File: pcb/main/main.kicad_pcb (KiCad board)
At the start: 2 copper layers, 91 x 94.8 mm, 71 parts, among them J1 XT60PW-M, J10 Conn, J11 Conn_ARM_JTAG_SWD_10, J12 UART1 SH, J13 Micro_SD_Card, J14 PH 2.0, J2 Conn_01x06_Female, J3 Conn_01x06_Female, J4 Conn_01x06_Female, J5 Conn_01x06_Female, J6 Conn_01x06_Female, J7 Conn_01x06_Female, J8 Conn, J9 Conn, Q1 BSS138, SW1 RESET, SW2 USER, U1 NJM12877F33-TE1, U2 STM32F405RGTx, U3 MCP2562-E-SN, U4 LXDC55FAAA-203, Y1 XRCGB16M000FXN02R0

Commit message: feat: finish main board v2
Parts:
- removed the C1 at (153.7, 116.5)
- removed the C2 at (151.7, 116.5)
- removed the R9 at (165.6, 95.2)
- removed the U1 at (148.2, 116.7)
- added D1: LED, LED_SMD:LED_0603_1608Metric, F.Cu at (143.2, 136.3)
- added H1: MountingHole, MountingHole:MountingHole_3.2mm_M3_Pad_TopBottom, F.Cu at (94.5, 51.3)
- added H2: MountingHole, MountingHole:MountingHole_3.2mm_M3_Pad_TopBottom, F.Cu at (179.5, 51.3)
- added H3: MountingHole, MountingHole:MountingHole_3.2mm_M3_Pad_TopBottom, F.Cu at (94.5, 140.1)
- added H4: MountingHole, MountingHole:MountingHole_3.2mm_M3_Pad_TopBottom, F.Cu at (179.5, 140.1)
- added H5: MountingHole, MountingHole:MountingHole_2.2mm_M2_ISO14580_Pad, F.Cu at (119.5, 103.4)
- added H6: MountingHole, MountingHole:MountingHole_2.2mm_M2_ISO14580_Pad, F.Cu at (138.1, 103.4)
- added H7: MountingHole, MountingHole:MountingHole_2.2mm_M2_ISO14580_Pad, F.Cu at (138.1, 130.1)
- added H8: MountingHole, MountingHole:MountingHole_2.2mm_M2_ISO14580_Pad, F.Cu at (119.5, 130.1)
- added R16: 120, Resistor_SMD:R_0603_1608Metric_Pad0.98x0.95mm_HandSolder, F.Cu at (164.8, 95.2)
- added R17: 120, Resistor_SMD:R_0603_1608Metric_Pad0.98x0.95mm_HandSolder, F.Cu at (94.2, 102.2)
- added R2: 1k, Resistor_SMD:R_0603_1608Metric_Pad0.98x0.95mm_HandSolder, F.Cu at (143.2, 139.6)
- added R25: 12k, Resistor_SMD:R_0603_1608Metric, F.Cu at (146.9, 125.5)
- added R26: 33k, Resistor_SMD:R_0603_1608Metric, F.Cu at (146.9, 122.4)
- added U2: LT1963AES3-3.3, Package_TO_SOT_SMD:SOT-223, F.Cu at (150.4, 111.6)
- C1: renamed from C17; moved to F.Cu
- C2: renamed from C18; footprint Capacitor_SMD:C_0603_1608Metric_Pad1.08x0.95mm_HandSolder -> Capacitor_SMD:C_0805_2012Metric_Pad1.18x1.45mm_HandSolder
- C3: value 0.01u -> 10u; footprint Capacitor_SMD:C_0603_1608Metric_Pad1.08x0.95mm_HandSolder -> Capacitor_SMD:C_0805_2012Metric_Pad1.18x1.45mm_HandSolder
- C4: value 1u -> 10u; footprint Capacitor_SMD:C_0603_1608Metric_Pad1.08x0.95mm_HandSolder -> Capacitor_SMD:C_0805_2012Metric_Pad1.18x1.45mm_HandSolder
- C5: renamed from C19; footprint Capacitor_SMD:C_0603_1608Metric_Pad1.08x0.95mm_HandSolder -> Capacitor_SMD:C_0805_2012Metric_Pad1.18x1.45mm_HandSolder
- D2: renamed from D1; footprint LED_SMD:LED_0402_1005Metric -> LED_SMD:LED_0603_1608Metric
- D3: renamed from D2; footprint LED_SMD:LED_0402_1005Metric -> LED_SMD:LED_0603_1608Metric
- D4: renamed from D3; footprint LED_SMD:LED_0402_1005Metric -> LED_SMD:LED_0603_1608Metric
- D5: renamed from D4; footprint LED_SMD:LED_0402_1005Metric -> LED_SMD:LED_0603_1608Metric
- D6: renamed from D5; footprint LED_SMD:LED_0402_1005Metric -> LED_SMD:LED_0603_1608Metric
- D7: renamed from D6; footprint LED_SMD:LED_0402_1005Metric -> LED_SMD:LED_0603_1608Metric
- D8: renamed from D7; footprint LED_SMD:LED_0402_1005Metric -> LED_SMD:LED_0603_1608Metric
- J1: footprint Connector_AMASS:AMASS_XT30U-F_1x02_P5.0mm_Vertical -> Connector_AMASS:AMASS_XT60PW-F_1x02_P7.20mm_Horizontal; moved to F.Cu
- J13: renamed from J11; footprint Connector_PinHeader_1.27mm:PinHeader_2x05_P1.27mm_Vertical -> mylib:322110010000
- J14: renamed from J12; footprint Connector_PinHeader_2.54mm:PinHeader_1x04_P2.54mm_Horizontal -> Connector_PinHeader_2.54mm:PinHeader_1x04_P2.54mm_Vertical
- R1: renamed from R22; footprint Resistor_SMD:R_0603_1608Metric_Pad0.98x0.95mm_HandSolder -> Resistor_SMD:R_0805_2012Metric
- moved SP1 58.4 mm to (89.8, 112.1), turned to 90 degrees
- moved R18 50.4 mm to (94.2, 103.7)
- moved Q1 50.4 mm to (94.2, 107.2)
- moved D6 19.7 mm to (135.9, 139.6)
- moved R15 19.7 mm to (135.9, 136.4)
- moved C1 18.5 mm to (160.4, 120.0), turned to 180 degrees
- moved C2 17.5 mm to (165.9, 113.4)
- moved C5 17.5 mm to (165.9, 109.9)
- moved R1 17.5 mm to (157.0, 110.6)
- moved U1 17.5 mm to (161.6, 111.5)
- moved D5 13.4 mm to (132.8, 139.7)
- moved R13 13.4 mm to (132.8, 136.4)
- moved J12 13.1 mm to (119.0, 117.1), turned to 90 degrees
- moved D2 12.7 mm to (140.6, 136.3), turned to 90 degrees
- moved J1 12.4 mm to (156.9, 127.2), turned to 180 degrees
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- renumbered C11 to C10, C12 to C11, C13 to C12, C14 to C13, C15 to C14, C5 to C15, C8 to C16, C16 to C17, C9 to C8, C10 to C9, J13 to J11, J14 to J12, R4 to R10, R5 to R11, R6 to R12, R7 to R13, R3 to R14, R8 to R15, R10 to R18, R11 to R19, R12 to R20, R13 to R21, R14 to R22, R15 to R23, R16 to R24, R1 to R3, R2 to R4, R17 to R5, R18 to R6, R19 to R7, R20 to R8, R21 to R9, U4 to U1, U2 to U3, U3 to U4
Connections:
- C3 pad 1: Net-(C3-Pad1) -> +5V
- J12 pad 1: +5V -> +3.3V
- Q1 pad 1: /stm32f405rg/TIM12_SP -> Net-(Q1-G)
- R18 pad 1: /stm32f405rg/TIM12_SP -> Net-(Q1-G)
- U3 pad 14: /stm32f405rg/SPI1_CS -> /stm32f405rg/SW1
- U3 pad 15: /stm32f405rg/LCD_RST -> /stm32f405rg/SPI1_CS
- U3 pad 16: /stm32f405rg/SW1 -> /stm32f405rg/LCD_RST
- U3 pad 27: /stm32f405rg/ADC1_IN9 -> /power/ADC_BATTERY
- U3 pad 33: unconnected-(U2-Pad33) -> /stm32f405rg/LED_CAN_RX
- U3 pad 34: /stm32f405rg/SPI2_SCK -> /imu/SPI_CLK
- U3 pad 36: unconnected-(U2-Pad36) -> /stm32f405rg/LED_CAN_TX
- U3 pad 38: /stm32f405rg/LED_CAN_RX -> unconnected-(U3-PC7-Pad38)
- U3 pad 41: /stm32f405rg/LED_CAN_TX -> unconnected-(U3-PA8-Pad41)
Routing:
- net GND: track 621.3 -> 99.7 mm, vias 103 -> 134
- net +3.3V: track 425.3 -> 348.7 mm, vias 9 -> 2
- net /stm32f405rg/NRST: track 144.6 -> 219.7 mm
- net /imu/SPI_MOSI: track 201.2 -> 167.0 mm, vias 2 -> 8
- net /power/ADC_BATTERY: track 0.00 -> 30.3 mm, vias 0 -> 2
- net +5V: track 141.7 -> 115.1 mm
- net /stm32f405rg/SWDIO: track 42.6 -> 62.9 mm, vias 1 -> 3
- net /stm32f405rg/LED4: track 61.6 -> 44.5 mm, vias 2 -> 0
- net /imu/SPI_MISO: track 194.6 -> 178.1 mm, vias 5 -> 9
- net /stm32f405rg/TIM3_LCD_BL: track 55.3 -> 39.4 mm
- net /stm32f405rg/LCD_DC: track 47.4 -> 32.9 mm
- net /stm32f405rg/LED3: track 57.7 -> 45.4 mm, vias 2 -> 0
- net /stm32f405rg/LCD_RST: track 45.1 -> 33.0 mm
- net /stm32f405rg/TIM12_SP: track 58.3 -> 70.1 mm, vias 2 -> 4
- net /imu/SPI_CLK: track 153.5 -> 164.8 mm, vias 4 -> 7
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- added copper zone on F.Cu, net +BATT
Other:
- outline, holes or cut-outs redrawn
- board text added: "3.3V"
- board text added: "5V"
- board text added: "GND"
- board text added: "RESET"
- board text added: "USART RX"
- board text added: "USART TX"
- board text added: "USER"

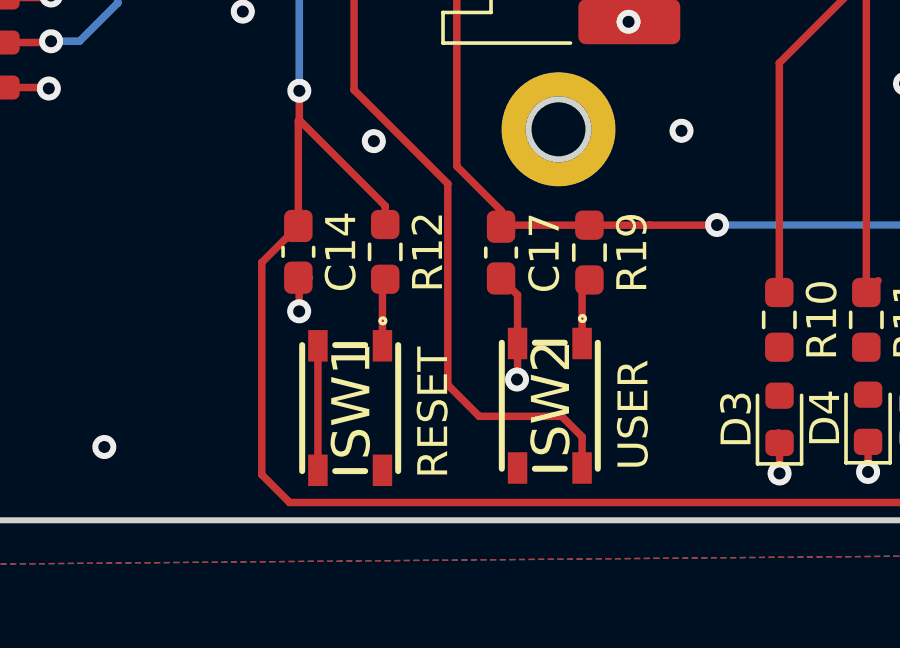
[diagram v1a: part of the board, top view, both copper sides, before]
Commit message: perf: edit SW footprint
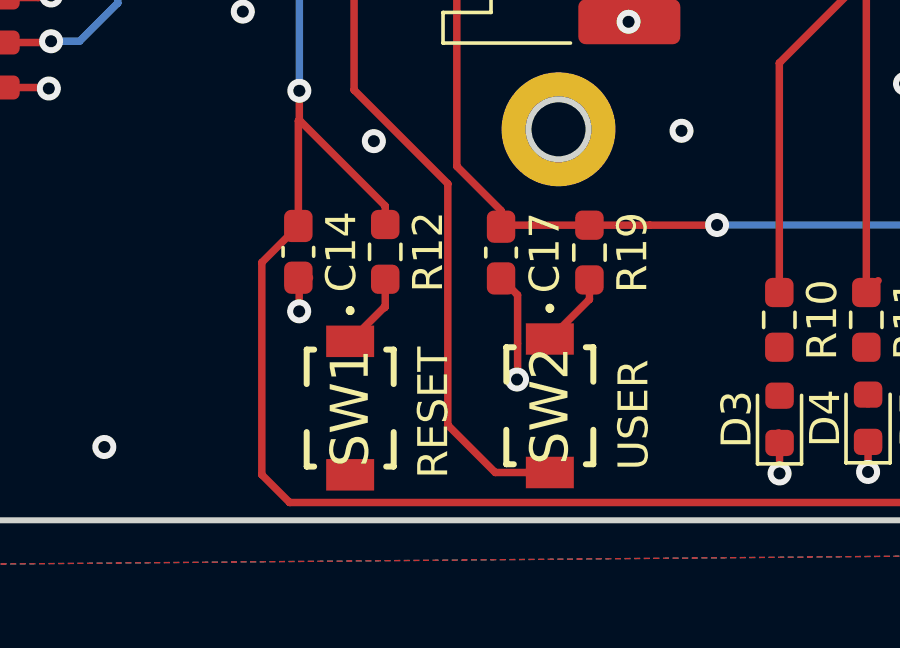
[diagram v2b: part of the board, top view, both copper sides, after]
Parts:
- SW1, SW2: footprint bldc_lib:SKRPACE010 -> mylib:TVAF06A020BR
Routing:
- net GND: track 99.7 -> 95.5 mm
- net /stm32f405rg/SW1: track 71.2 -> 70.4 mm
- net Net-(R19-Pad2): track 2.22 -> 2.86 mm

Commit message: feat: delete two CAN connectors & add microSD input pin
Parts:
- removed the J10 at (174.0, 95.3)
- removed the J11 at (162.5, 57.1)
- added G***: LOGO, mylib:science_tokyo_logo, F.Cu at (115.9, 76.4)
- added G***: LOGO, mylib:tokyotech_logo, B.Cu at (116.0, 76.4)
- J1: value XT60PW-M -> XT30PW-M; footprint Connector_AMASS:AMASS_XT60PW-F_1x02_P7.20mm_Horizontal -> Connector_AMASS:AMASS_XT30PW-M_1x02_P2.50mm_Horizontal
- J9: value Conn -> Micro_SD_Card_Det_Hirose_DM3AT; footprint bldc_lib:21322604YY -> Connector_Card:microSD_HC_Hirose_DM3AT-SF-PEJM5
- moved J9 54.7 mm to (162.4, 56.8), turned to 180 degrees
- moved J8 30.1 mm to (172.1, 95.3)
- moved D1 13.4 mm to (156.6, 136.2)
- moved D2 13.4 mm to (154.0, 136.2)
- moved R5 13.4 mm to (154.0, 139.5)
- moved R4 13.4 mm to (156.6, 139.5)
- moved D5 13.3 mm to (146.1, 139.6)
- moved D6 13.3 mm to (149.2, 139.5)
- moved R12 13.3 mm to (140.2, 136.3)
- moved R13 13.3 mm to (143.1, 136.3)
- moved R15 13.3 mm to (146.1, 136.3)
- moved R17 13.3 mm to (149.2, 136.3)
- moved D3 13.3 mm to (140.2, 139.6)
- moved D4 13.3 mm to (143.1, 139.6)
- moved R2 10.1 mm to (156.2, 129.4)
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- renumbered J12 to J10, J13 to J11, J14 to J12, R8 to R10, R9 to R11, R10 to R12, R11 to R13, R12 to R14, R13 to R15, R14 to R16, R15 to R17, R16 to R18, R17 to R19, R25 to R2, R18 to R20, R19 to R21, R20 to R22, R21 to R23, R22 to R24, R23 to R25, R24 to R26, R26 to R3, R2 to R4, R3 to R5, R4 to R6, R5 to R7, R6 to R8, R7 to R9
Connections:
- J9 pad 1: +5V -> /stm32f405rg/SDIO_D2
- J9 pad 2: /can/CAN_L -> /stm32f405rg/SDIO_D3
- J9 pad 3: /can/CAN_H -> /stm32f405rg/SDIO_CMD
- J9 pad 4: GND -> +3.3V
- J9 pad 5: GND -> /stm32f405rg/SDIO_CK
- U3 pad 15: /stm32f405rg/SPI1_CS -> unconnected-(U3-PA1-Pad15)
- U3 pad 16: /stm32f405rg/LCD_RST -> /stm32f405rg/LCD_DC
- U3 pad 17: /stm32f405rg/LCD_DC -> /stm32f405rg/SPI1_CS
- U3 pad 50: unconnected-(U3-PA15-Pad50) -> /stm32f405rg/SDIO_SW
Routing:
- net /can/CAN_L: track 54.9 -> 9.87 mm
- net /can/CAN_H: track 51.3 -> 9.75 mm
- net /stm32f405rg/SDIO_SW: track 0.00 -> 40.2 mm, vias 0 -> 2
- net +5V: track 115.1 -> 78.2 mm
- net +3.3V: track 348.7 -> 372.1 mm
- net /stm32f405rg/NRST: track 219.7 -> 233.7 mm
- net /stm32f405rg/SPI1_CS: track 42.7 -> 34.1 mm
- net GND: track 95.5 -> 87.8 mm, vias 134 -> 122
- net /power/ADC_BATTERY: track 30.3 -> 37.9 mm
- net /stm32f405rg/LED2: track 46.3 -> 40.2 mm
- net +BATT: track 31.1 -> 25.5 mm
- net /stm32f405rg/LED1: track 46.8 -> 41.1 mm
- net /stm32f405rg/LED3: track 45.4 -> 39.9 mm
- net /stm32f405rg/LED4: track 44.5 -> 40.9 mm
- net /stm32f405rg/SDIO_D2: track 25.1 -> 27.2 mm
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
